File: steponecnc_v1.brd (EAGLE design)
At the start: 101.6 x 83.8 mm, 32 parts

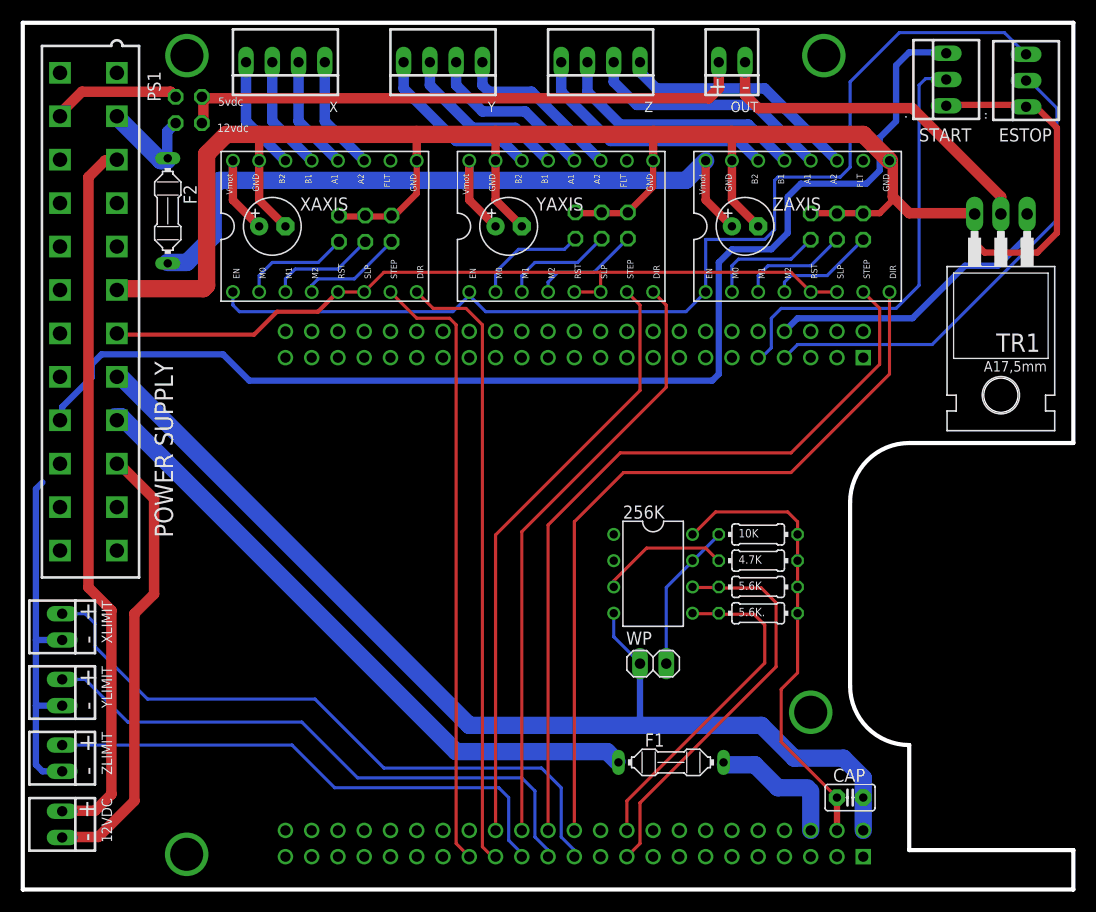
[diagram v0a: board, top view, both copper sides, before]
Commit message: updates to bom/eagle file
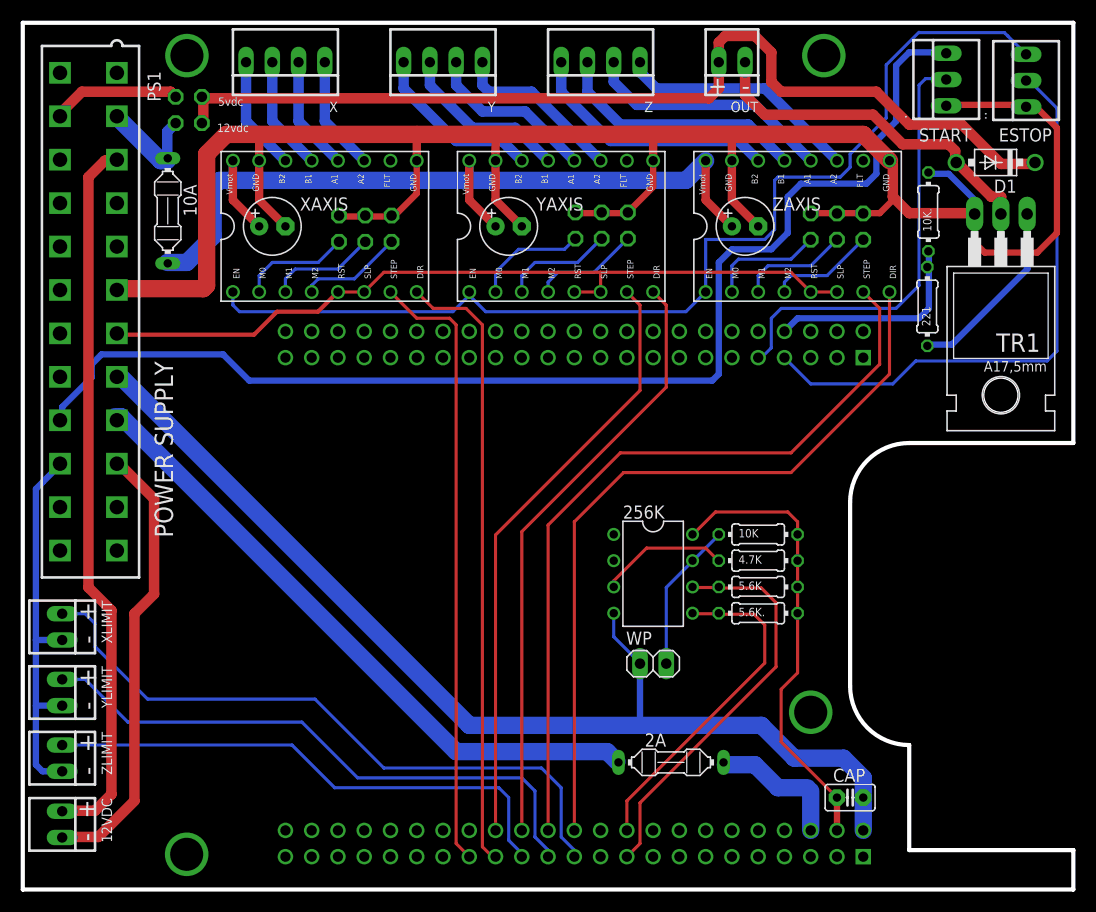
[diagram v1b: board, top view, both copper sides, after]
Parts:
- added 10K., 221: (no value), resistor2:0204/7
- added D1: (no value), diode:DO41-7
- renumbered F1 to 2A, F2 to 10A
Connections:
- net S$11 renamed S$71
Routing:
- net S$58: track 55.0 -> 94.5 mm
- net S$70: track 0.00 -> 17.9 mm
- net S$27: track 102.4 -> 89.9 mm
- net S$69: track 0.00 -> 11.4 mm
- net S$71: track 46.7 -> 56.3 mm
- net S$38: track 29.5 -> 20.3 mm
- net S$11: track 0.00 -> 7.08 mm
- net S$39: track 35.5 -> 38.1 mm
- net S$34: track 33.6 -> 34.2 mm
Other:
- board text added: "StepOneCNC v1.0 © 2014 GPL v3.0"
- board text removed: "DPE v1.0"
